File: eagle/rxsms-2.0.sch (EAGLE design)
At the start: 145 parts, among them Q1 opt, Q10 BSS123, Q11 BSS123, Q12 BSS123, Q2 BSS123, Q3 BSS123, Q4 BSS123, Q5 BSS123, Q6 BSS123, Q7 BSS123, Q8 BSS123, Q9 BSS123, T1 SMS_IP67, T10 SWITCH_LED, T2 SMS_IP67, T3 SWITCH_LED, T4 SMS_IP67, T5 SMS_IP67, T6 SWITCH_LED, T7 SWITCH_LED, T8 SWITCH_LED, T9 SMS_IP67, U1 MAX3232ESE, U2 XMEGA-A4UTQFP, U3 TSR_1-2450, U4 LM1117, U5 TMV_0505EN, U6 ADUM3160, U7 TPS73125, U8 NUP2202W1, X1 PN61729-S, X5 RLP2-200-500

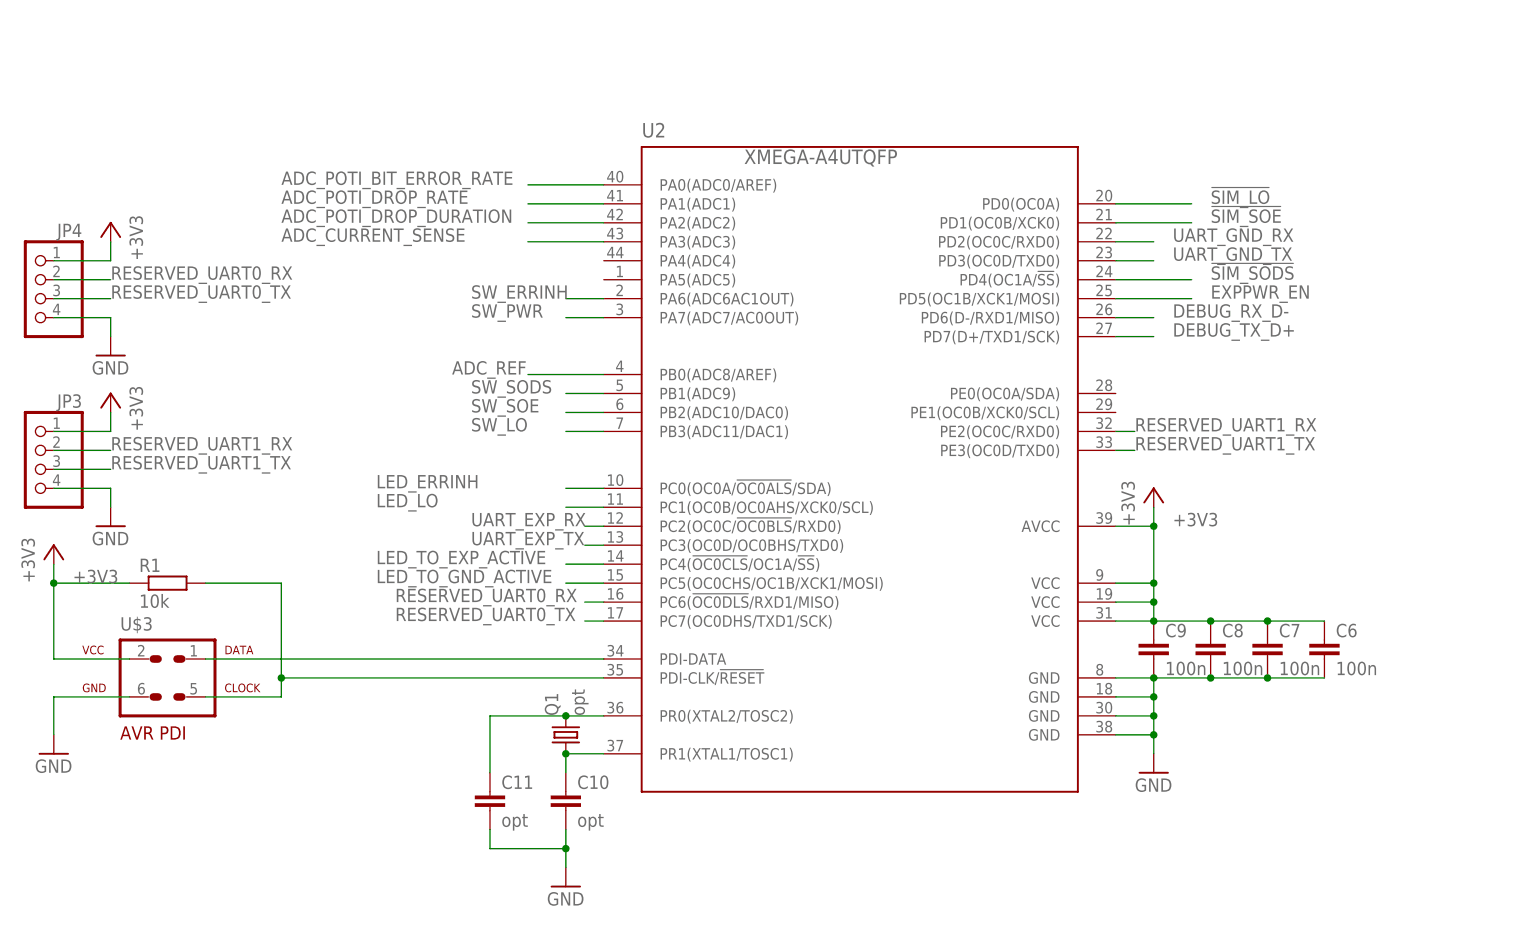
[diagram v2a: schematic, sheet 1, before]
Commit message: add pinheaders for reserved ADC and GPIO pins
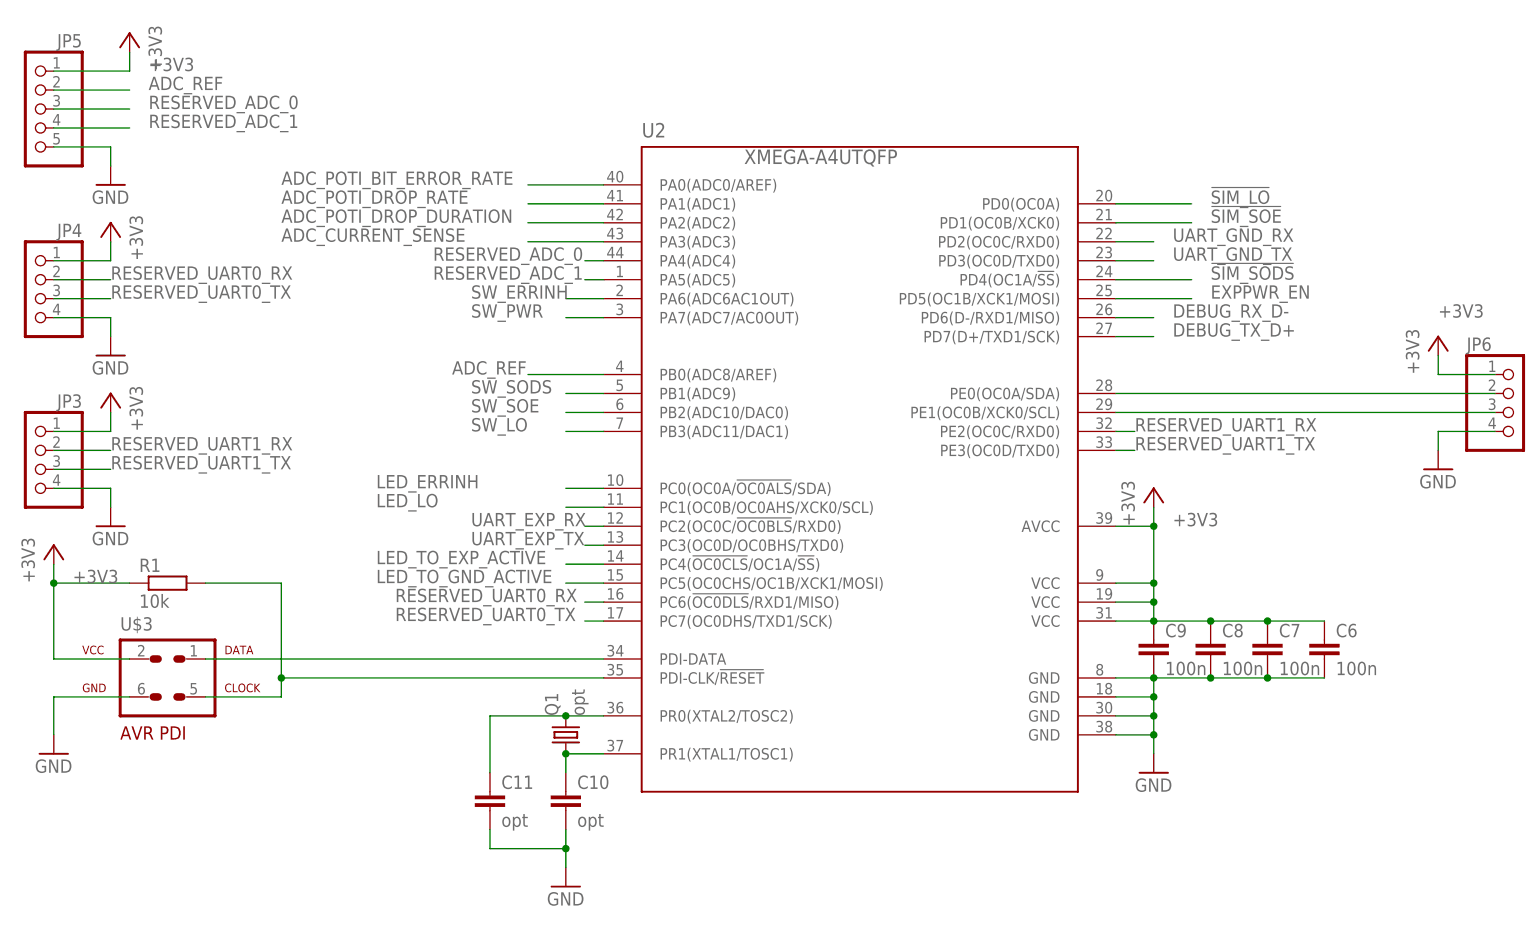
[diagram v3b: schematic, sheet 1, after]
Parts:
- added JP5: (no value), pinhead:PINHD-1X5
- added JP6: (no value), pinhead:PINHD-1X4
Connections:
- new net N$33: JP6.2, U2.PE0(OC0A/SDA)
- new net N$36: JP6.3, U2.PE1(OC0B/XCK0/SCL)
- new net RESERVED_ADC_0: U2.PA4(ADC4)
- new net RESERVED_ADC_1: U2.PA5(ADC5)
- net +3V3: now also JP5.1, JP6.1
- net GND: now also JP5.5, JP6.4
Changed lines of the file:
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@@
 <part name="+3V14" library="supply1" deviceset="+3V3" device=""/>
 <part name="+3V15" library="supply1" deviceset="+3V3" device=""/>
+<part name="JP5" library="pinhead" deviceset="PINHD-1X5" device=""/>
+<part name="GND36" library="supply1" deviceset="GND" device=""/>
+<part name="+3V16" library="supply1" deviceset="+3V3" device=""/>
+<part name="JP6" library="pinhead" deviceset="PINHD-1X4" device=""/>
+<part name="GND37" library="supply1" deviceset="GND" device=""/>
+<part name="+3V17" library="supply1" deviceset="+3V3" device=""/>
 </parts>
 <sheets>
@@
 <instance part="+3V14" gate="G$1" x="22.86" y="111.76" rot="MR0"/>
 <instance part="+3V15" gate="G$1" x="22.86" y="134.62" rot="MR0"/>
+<instance part="JP5" gate="A" x="12.7" y="149.86" rot="MR0"/>
+<instance part="GND36" gate="1" x="22.86" y="139.7"/>
+<instance part="+3V16" gate="G$1" x="25.4" y="160.02" rot="MR0"/>
+<instance part="JP6" gate="A" x="210.82" y="109.22"/>
+<instance part="GND37" gate="1" x="200.66" y="101.6"/>
+<instance part="+3V17" gate="G$1" x="200.66" y="119.38"/>
 </instances>
 <busses>
@@
 <pinref part="+3V15" gate="G$1" pin="+3V3"/>
 </segment>
+<segment>
+<pinref part="JP5" gate="A" pin="1"/>
+<pinref part="+3V16" gate="G$1" pin="+3V3"/>
+<wire x1="15.24" y1="154.94" x2="25.4" y2="154.94" width="0.1524" layer="91"/>
+<wire x1="25.4" y1="154.94" x2="25.4" y2="157.48" width="0.1524" layer="91"/>
+<label x="27.94" y="154.94" size="1.778" layer="95"/>
+</segment>
+<segment>
+<pinref part="JP6" gate="A" pin="1"/>
+<pinref part="+3V17" gate="G$1" pin="+3V3"/>
+<wire x1="208.28" y1="114.3" x2="200.66" y2="114.3" width="0.1524" layer="91"/>
+<wire x1="200.66" y1="114.3" x2="200.66" y2="116.84" width="0.1524" layer="91"/>
+<label x="200.66" y="121.92" size="1.778" layer="95"/>
+</segment>
 </net>
 <net name="GND" class="0">
@@
 <pinref part="GND35" gate="1" pin="GND"/>
 </segment>
+<segment>
+<pinref part="JP5" gate="A" pin="5"/>
+<pinref part="GND36" gate="1" pin="GND"/>
+<wire x1="15.24" y1="144.78" x2="22.86" y2="144.78" width="0.1524" layer="91"/>
+<wire x1="22.86" y1="144.78" x2="22.86" y2="142.24" width="0.1524" layer="91"/>
+</segment>
+<segment>
+<pinref part="JP6" gate="A" pin="4"/>
+<pinref part="GND37" gate="1" pin="GND"/>
+<wire x1="208.28" y1="106.68" x2="200.66" y2="106.68" width="0.1524" layer="91"/>
+<wire x1="200.66" y1="106.68" x2="200.66" y2="104.14" width="0.1524" layer="91"/>
+</segment>
 </net>
 <net name="N$11" class="0">
@@
 <label x="68.58" y="114.3" size="1.778" layer="95"/>
 </segment>
+<segment>
+<wire x1="25.4" y1="152.4" x2="15.24" y2="152.4" width="0.1524" layer="91"/>
+<label x="27.94" y="152.4" size="1.778" layer="95"/>
+</segment>
 </net>
 <net name="DEBUG_RX_D-" class="0">
@@
 </segment>
 </net>
+<net name="RESERVED_ADC_0" class="0">
+<segment>
+<pinref part="U2" gate="G$1" pin="PA4(ADC4)"/>
+<wire x1="88.9" y1="129.54" x2="86.36" y2="129.54" width="0.1524" layer="91"/>
+<label x="66.04" y="129.54" size="1.778" layer="95"/>
+</segment>
+<segment>
+<wire x1="25.4" y1="149.86" x2="15.24" y2="149.86" width="0.1524" layer="91"/>
+<label x="27.94" y="149.86" size="1.778" layer="95"/>
+</segment>
+</net>
+<net name="RESERVED_ADC_1" class="0">
+<segment>
+<pinref part="U2" gate="G$1" pin="PA5(ADC5)"/>
+<wire x1="88.9" y1="127" x2="86.36" y2="127" width="0.1524" layer="91"/>
+<label x="66.04" y="127" size="1.778" layer="95"/>
+</segment>
+<segment>
+<wire x1="25.4" y1="147.32" x2="15.24" y2="147.32" width="0.1524" layer="91"/>
+<label x="27.94" y="147.32" size="1.778" layer="95"/>
+</segment>
+</net>
+<net name="N$33" class="0">
+<segment>
+<pinref part="U2" gate="G$1" pin="PE0(OC0A/SDA)"/>
+<wire x1="157.48" y1="111.76" x2="208.28" y2="111.76" width="0.1524" layer="91"/>
+<pinref part="JP6" gate="A" pin="2"/>
+</segment>
+</net>
+<net name="N$36" class="0">
+<segment>
+<pinref part="U2" gate="G$1" pin="PE1(OC0B/XCK0/SCL)"/>
+<pinref part="JP6" gate="A" pin="3"/>
+<wire x1="157.48" y1="109.22" x2="208.28" y2="109.22" width="0.1524" layer="91"/>
+</segment>
+</net>

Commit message: add power supply connectors
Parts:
- added SV1: (no value), con-harting-ml:ML26L
- added X6: (no value), con-ptr500:AK500/2
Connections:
- new net N$67: SV1.10, SV1.12, SV1.14, SV1.4, SV1.6, SV1.8
- new net N$69: SV1.11, SV1.13, SV1.3, SV1.5, SV1.7, SV1.9
- net +28V_SUPPLY: now also SV1.15, SV1.16, SV1.17, SV1.18, SV1.19, SV1.20, SV1.21, SV1.22, SV1.23, SV1.24, SV1.25, SV1.26, X6-1.KL
- net GND: now also X6-2.KL
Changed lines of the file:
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@@
 <part name="GND37" library="supply1" deviceset="GND" device=""/>
 <part name="+3V17" library="supply1" deviceset="+3V3" device=""/>
+<part name="SV1" library="con-harting-ml" deviceset="ML26" device="L"/>
+<part name="FRAME8" library="frames" deviceset="DINA4_L" device=""/>
+<part name="P+13" library="supply1" deviceset="+24V" device="" value="+28V_SUPPLY"/>
+<part name="GND38" library="supply1" deviceset="GND" device=""/>
+<part name="GND39" library="supply1" deviceset="GND" device=""/>
+<part name="P+14" library="supply1" deviceset="+24V" device="" value="+28V_SUPPLY"/>
+<part name="X6" library="con-ptr500" deviceset="AK500/2" device=""/>
+<part name="P+15" library="supply1" deviceset="+24V" device="" value="+28V_SUPPLY"/>
+<part name="GND40" library="supply1" deviceset="GND" device=""/>
 </parts>
 <sheets>
@@
 <instance part="GND5" gate="1" x="78.74" y="104.14"/>
 <instance part="GND6" gate="1" x="124.46" y="104.14"/>
-<instance part="P+2" gate="1" x="45.72" y="134.62"/>
+<instance part="P+2" gate="1" x="53.34" y="134.62"/>
 <instance part="GND7" gate="1" x="45.72" y="106.68"/>
 <instance part="P+3" gate="1" x="93.98" y="134.62"/>
@@
 <segment>
 <pinref part="P+2" gate="1" pin="+24V"/>
-<wire x1="45.72" y1="132.08" x2="45.72" y2="124.46" width="0.1524" layer="91"/>
-<wire x1="45.72" y1="124.46" x2="53.34" y2="124.46" width="0.1524" layer="91"/>
+<wire x1="53.34" y1="132.08" x2="53.34" y2="119.38" width="0.1524" layer="91"/>
 <pinref part="C12" gate="G$1" pin="1"/>
-<wire x1="53.34" y1="124.46" x2="53.34" y2="119.38" width="0.1524" layer="91"/>
-<label x="48.26" y="132.08" size="1.778" layer="95"/>
+<label x="55.88" y="132.08" size="1.778" layer="95"/>
 </segment>
 </net>
@@
 </segment>
 </net>
+</nets>
+</sheet>
+<sheet>
+<plain>
+</plain>
+<instances>
+<instance part="SV1" gate="1" x="124.46" y="111.76"/>
+<instance part="FRAME8" gate="G$1" x="0" y="0"/>
+<instance part="FRAME8" gate="G$2" x="162.56" y="0"/>
+<instance part="P+13" gate="1" x="114.3" y="137.16"/>
+<instance part="GND38" gate="1" x="109.22" y="101.6" rot="R270"/>
+<instance part="GND39" gate="1" x="139.7" y="101.6" rot="R90"/>
+<instance part="P+14" gate="1" x="134.62" y="137.16"/>
+<instance part="X6" gate="-1" x="60.96" y="119.38"/>
+<instance part="X6" gate="-2" x="60.96" y="114.3"/>
+<instance part="P+15" gate="1" x="68.58" y="129.54"/>
+<instance part="GND40" gate="1" x="68.58" y="109.22"/>
+</instances>
+<busses>
+</busses>
+<nets>
+<net name="!SIM_LO" class="0">
+<segment>
+<wire x1="132.08" y1="96.52" x2="142.24" y2="96.52" width="0.1524" layer="91"/>
+<label x="144.78" y="96.52" size="1.778" layer="95"/>
+</segment>
+</net>
+<net name="!EXP_LO" class="0">
+<segment>
+<wire x1="116.84" y1="96.52" x2="106.68" y2="96.52" width="0.1524" layer="91"/>
+<label x="91.44" y="96.52" size="1.778" layer="95"/>
+</segment>
+</net>
+<net name="+28V_SUPPLY" class="0">
+<segment>
+<pinref part="P+13" gate="1" pin="+24V"/>
+<wire x1="114.3" y1="134.62" x2="114.3" y2="127" width="0.1524" layer="91"/>
+<label x="111.76" y="127" size="1.778" layer="95" rot="MR0"/>
+<pinref part="SV1" gate="1" pin="16"/>
+<wire x1="116.84" y1="114.3" x2="114.3" y2="114.3" width="0.1524" layer="91"/>
+<wire x1="114.3" y1="114.3" x2="114.3" y2="116.84" width="0.1524" layer="91"/>
+<pinref part="SV1" gate="1" pin="26"/>
+<wire x1="114.3" y1="116.84" x2="114.3" y2="119.38" width="0.1524" layer="91"/>
+<wire x1="114.3" y1="119.38" x2="114.3" y2="121.92" width="0.1524" layer="91"/>
+<wire x1="114.3" y1="121.92" x2="114.3" y2="124.46" width="0.1524" layer="91"/>
+<wire x1="114.3" y1="124.46" x2="114.3" y2="127" width="0.1524" layer="91"/>
+<wire x1="116.84" y1="127" x2="114.3" y2="127" width="0.1524" layer="91"/>
+<pinref part="SV1" gate="1" pin="18"/>
+<wire x1="116.84" y1="116.84" x2="114.3" y2="116.84" width="0.1524" layer="91"/>
+<junction x="114.3" y="116.84"/>
+<pinref part="SV1" gate="1" pin="20"/>
+<wire x1="114.3" y1="119.38" x2="116.84" y2="119.38" width="0.1524" layer="91"/>
+<junction x="114.3" y="119.38"/>
+<pinref part="SV1" gate="1" pin="22"/>
+<wire x1="116.84" y1="121.92" x2="114.3" y2="121.92" width="0.1524" layer="91"/>
+<junction x="114.3" y="121.92"/>
+<pinref part="SV1" gate="1" pin="24"/>
+<wire x1="114.3" y1="124.46" x2="116.84" y2="124.46" width="0.1524" layer="91"/>
+<junction x="114.3" y="124.46"/>
+<junction x="114.3" y="127"/>
+</segment>
+<segment>
+<pinref part="P+14" gate="1" pin="+24V"/>
+<wire x1="134.62" y1="134.62" x2="134.62" y2="127" width="0.1524" layer="91"/>
+<label x="137.16" y="127" size="1.778" layer="95"/>
+<pinref part="SV1" gate="1" pin="25"/>
+<wire x1="132.08" y1="127" x2="134.62" y2="127" width="0.1524" layer="91"/>
+<wire x1="134.62" y1="127" x2="134.62" y2="124.46" width="0.1524" layer="91"/>
+<pinref part="SV1" gate="1" pin="15"/>
+<wire x1="134.62" y1="124.46" x2="134.62" y2="121.92" width="0.1524" layer="91"/>
+<wire x1="134.62" y1="121.92" x2="134.62" y2="119.38" width="0.1524" layer="91"/>
+<wire x1="134.62" y1="119.38" x2="134.62" y2="116.84" width="0.1524" layer="91"/>
+<wire x1="134.62" y1="116.84" x2="134.62" y2="114.3" width="0.1524" layer="91"/>
+<wire x1="134.62" y1="114.3" x2="132.08" y2="114.3" width="0.1524" layer="91"/>
+<pinref part="SV1" gate="1" pin="17"/>
+<wire x1="132.08" y1="116.84" x2="134.62" y2="116.84" width="0.1524" layer="91"/>
+<junction x="134.62" y="116.84"/>
+<pinref part="SV1" gate="1" pin="19"/>
+<wire x1="134.62" y1="119.38" x2="132.08" y2="119.38" width="0.1524" layer="91"/>
+<junction x="134.62" y="119.38"/>
+<pinref part="SV1" gate="1" pin="21"/>
+<wire x1="132.08" y1="121.92" x2="134.62" y2="121.92" width="0.1524" layer="91"/>
+<junction x="134.62" y="121.92"/>
+<pinref part="SV1" gate="1" pin="23"/>
+<wire x1="134.62" y1="124.46" x2="132.08" y2="124.46" width="0.1524" layer="91"/>
+<junction x="134.62" y="124.46"/>
+<junction x="134.62" y="127"/>
+</segment>
+<segment>
+<pinref part="X6" gate="-1" pin="KL"/>
+<pinref part="P+15" gate="1" pin="+24V"/>
+<wire x1="66.04" y1="119.38" x2="68.58" y2="119.38" width="0.1524" layer="91"/>
+<wire x1="68.58" y1="119.38" x2="68.58" y2="127" width="0.1524" layer="91"/>
+<label x="71.12" y="119.38" size="1.778" layer="95"/>
+</segment>
+</net>
+<net name="N$67" class="0">
+<segment>
+<pinref part="SV1" gate="1" pin="4"/>
+<wire x1="116.84" y1="99.06" x2="114.3" y2="99.06" width="0.1524" layer="91"/>
+<wire x1="114.3" y1="99.06" x2="114.3" y2="101.6" width="0.1524" layer="91"/>
+<pinref part="SV1" gate="1" pin="14"/>
+<wire x1="114.3" y1="101.6" x2="114.3" y2="104.14" width="0.1524" layer="91"/>
+<wire x1="114.3" y1="104.14" x2="114.3" y2="106.68" width="0.1524" layer="91"/>
+<wire x1="114.3" y1="106.68" x2="114.3" y2="109.22" width="0.1524" layer="91"/>
+<wire x1="114.3" y1="109.22" x2="114.3" y2="111.76" width="0.1524" layer="91"/>
+<wire x1="114.3" y1="111.76" x2="116.84" y2="111.76" width="0.1524" layer="91"/>
+<pinref part="SV1" gate="1" pin="12"/>
+<wire x1="116.84" y1="109.22" x2="114.3" y2="109.22" width="0.1524" layer="91"/>
+<junction x="114.3" y="109.22"/>
+<pinref part="SV1" gate="1" pin="10"/>
+<wire x1="116.84" y1="106.68" x2="114.3" y2="106.68" width="0.1524" layer="91"/>
+<junction x="114.3" y="106.68"/>
+<pinref part="SV1" gate="1" pin="8"/>
+<wire x1="116.84" y1="104.14" x2="114.3" y2="104.14" width="0.1524" layer="91"/>
+<junction x="114.3" y="104.14"/>
+<pinref part="SV1" gate="1" pin="6"/>
+<wire x1="116.84" y1="101.6" x2="114.3" y2="101.6" width="0.1524" layer="91"/>
+<junction x="114.3" y="101.6"/>
+</segment>
+</net>
+<net name="N$69" class="0">
+<segment>
+<pinref part="SV1" gate="1" pin="13"/>
+<wire x1="132.08" y1="111.76" x2="134.62" y2="111.76" width="0.1524" layer="91"/>
+<wire x1="134.62" y1="111.76" x2="134.62" y2="109.22" width="0.1524" layer="91"/>
+<pinref part="SV1" gate="1" pin="3"/>
+<wire x1="134.62" y1="109.22" x2="134.62" y2="106.68" width="0.1524" layer="91"/>
+<wire x1="134.62" y1="106.68" x2="134.62" y2="104.14" width="0.1524" layer="91"/>
+<wire x1="134.62" y1="104.14" x2="134.62" y2="101.6" width="0.1524" layer="91"/>
+<wire x1="134.62" y1="101.6" x2="134.62" y2="99.06" width="0.1524" layer="91"/>
+<wire x1="134.62" y1="99.06" x2="132.08" y2="99.06" width="0.1524" layer="91"/>
+<pinref part="SV1" gate="1" pin="5"/>
+<wire x1="132.08" y1="101.6" x2="134.62" y2="101.6" width="0.1524" layer="91"/>
+<junction x="134.62" y="101.6"/>
+<pinref part="SV1" gate="1" pin="7"/>
+<wire x1="134.62" y1="104.14" x2="132.08" y2="104.14" width="0.1524" layer="91"/>
+<junction x="134.62" y="104.14"/>
+<pinref part="SV1" gate="1" pin="9"/>
+<wire x1="132.08" y1="106.68" x2="134.62" y2="106.68" width="0.1524" layer="91"/>
+<junction x="134.62" y="106.68"/>
+<pinref part="SV1" gate="1" pin="11"/>
+<wire x1="134.62" y1="109.22" x2="132.08" y2="109.22" width="0.1524" layer="91"/>
+<junction x="134.62" y="109.22"/>
+</segment>
+</net>
+<net name="GND" class="0">
+<segment>
+<pinref part="GND38" gate="1" pin="GND"/>
+<wire x1="114.3" y1="101.6" x2="111.76" y2="101.6" width="0.1524" layer="91"/>
+</segment>
+<segment>
+<pinref part="GND39" gate="1" pin="GND"/>
+<wire x1="134.62" y1="101.6" x2="137.16" y2="101.6" width="0.1524" layer="91"/>
+</segment>
+<segment>
+<pinref part="X6" gate="-2" pin="KL"/>
+<pinref part="GND40" gate="1" pin="GND"/>
+<wire x1="66.04" y1="114.3" x2="68.58" y2="114.3" width="0.1524" layer="91"/>
+<wire x1="68.58" y1="114.3" x2="68.58" y2="111.76" width="0.1524" layer="91"/>
+</segment>
+</net>
